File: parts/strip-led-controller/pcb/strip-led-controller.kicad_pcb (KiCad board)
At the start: 2 copper layers, 100.5 x 48 mm, 18 parts, among them J1 BUCK_IN, J2 PWR IN, J3 BUCK_OUT, SW2 SW_SPDT, U1 ESP32 Wemos D1 Mini

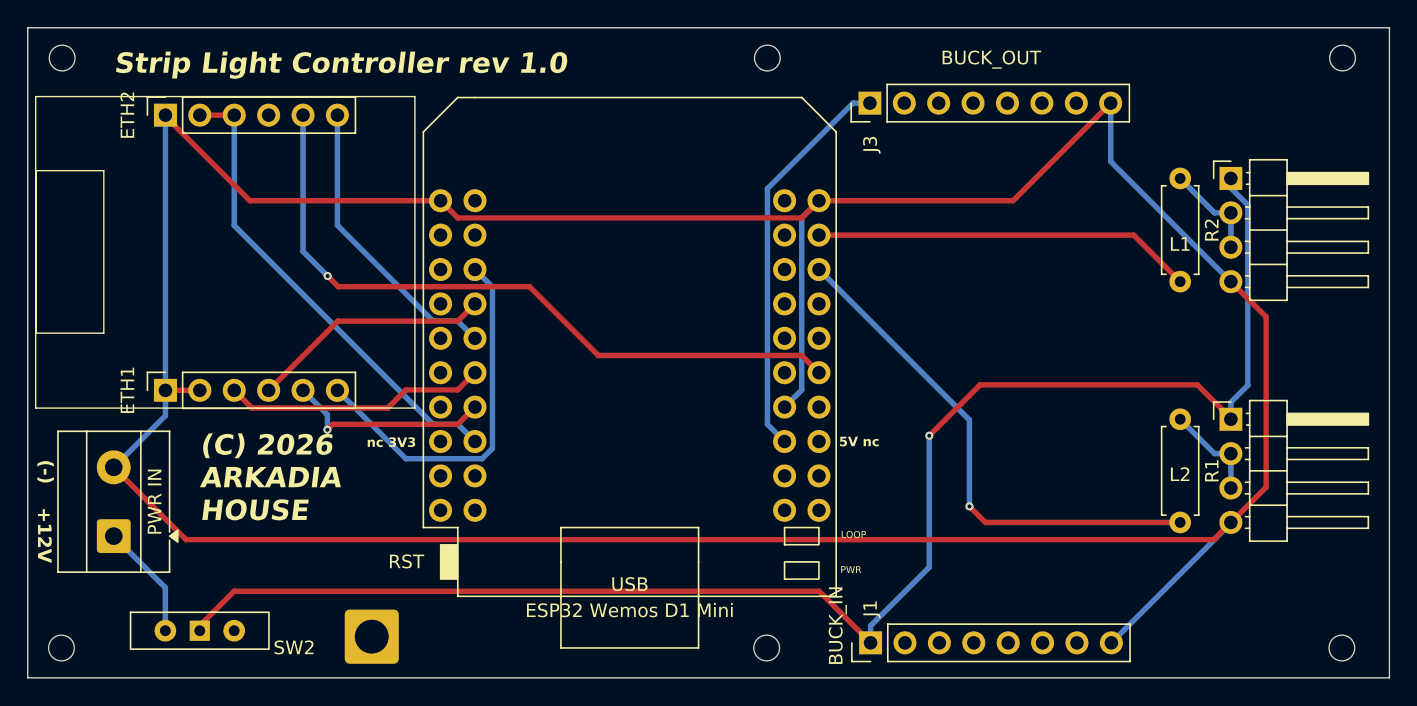
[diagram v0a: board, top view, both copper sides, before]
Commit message: update RJ45 connector to "clip up" model
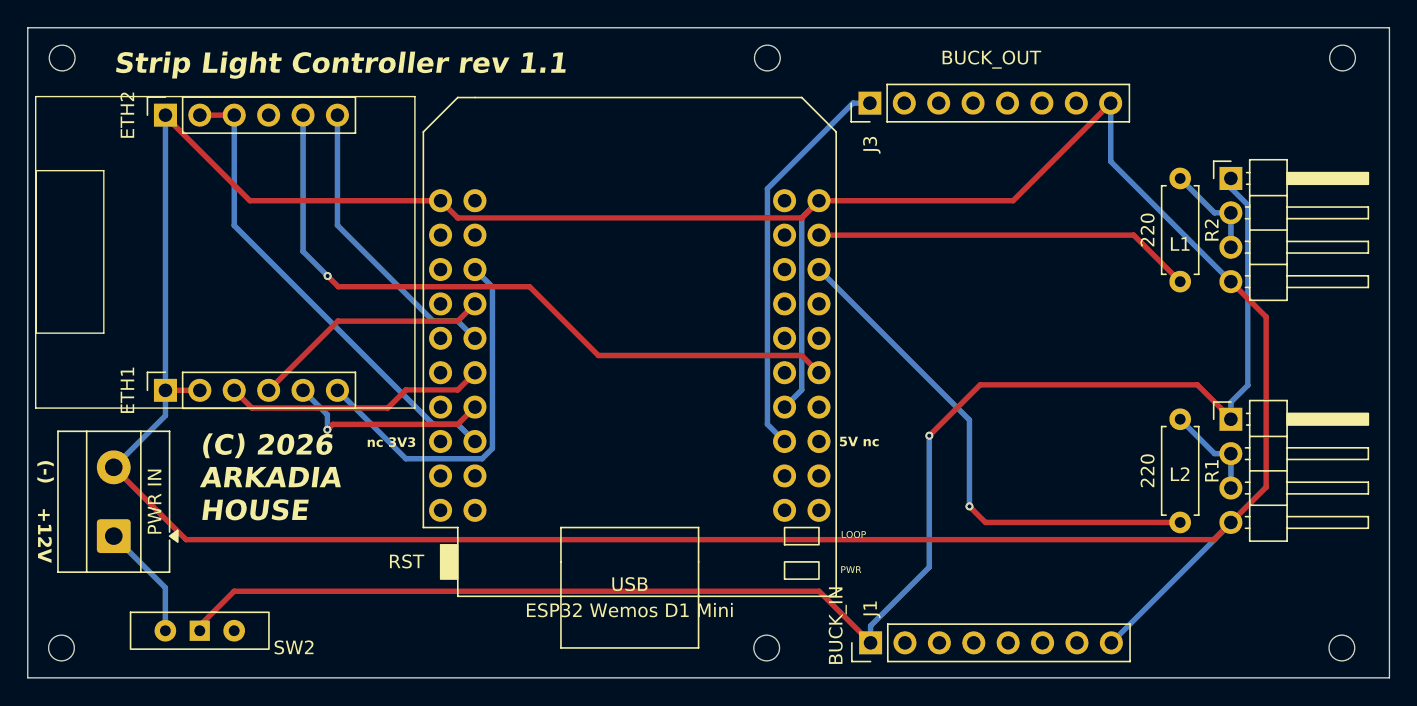
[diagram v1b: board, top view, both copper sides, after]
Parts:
- removed SHIELD1: Conn_01x01_Shielded, TerminalBlock:TerminalBlock_MaiXu_MX126-5.0-02P_1x02_P5.00mm
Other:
- board text added: "Strip Light Controller rev 1.1"
- board text removed: "Strip Light Controller rev 1.0"

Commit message: pixelstrip controller 1.2 adjusts small geometry and labeling based on assembly esperience.
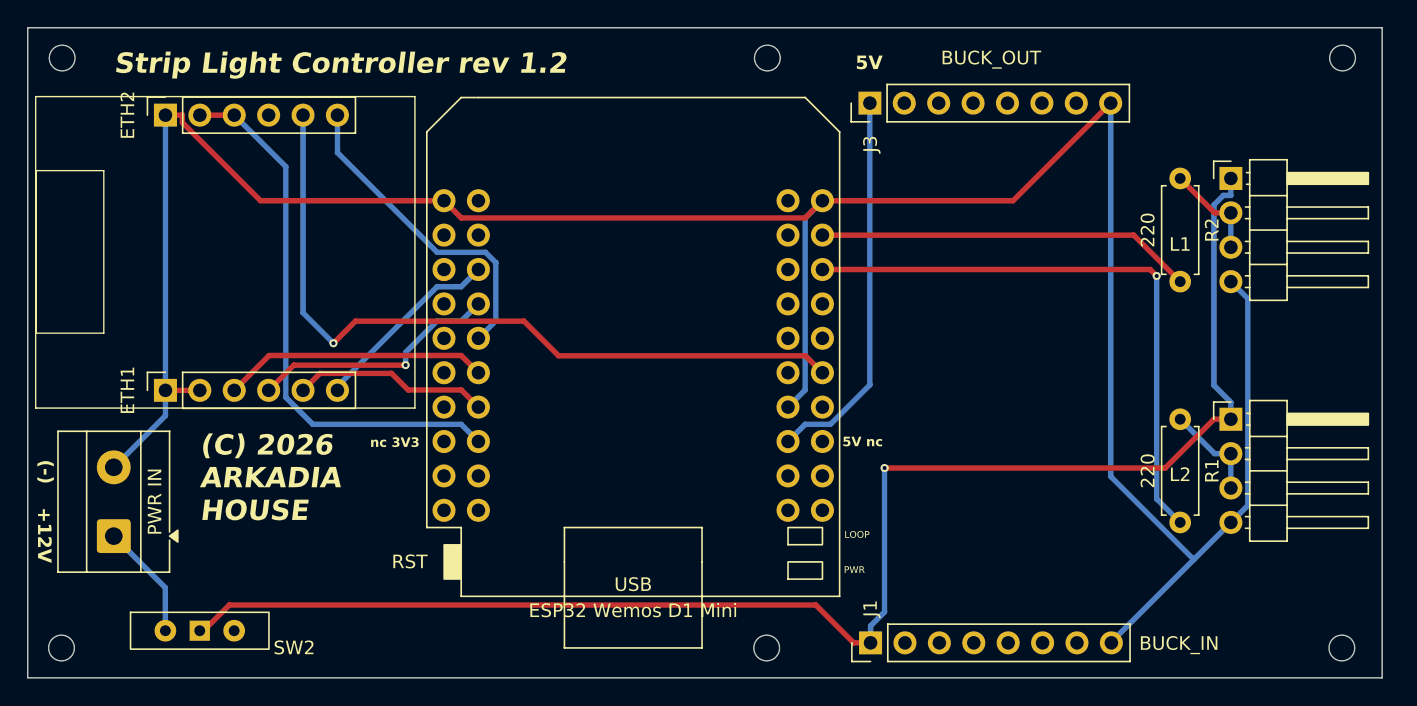
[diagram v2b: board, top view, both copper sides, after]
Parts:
- moved U1 0.25 mm to (68.2, 46.4)
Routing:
- net GND: track 257.4 -> 190.7 mm
- net /INT: track 27.6 -> 14.0 mm
- net Net-(U1-IO_25): track 38.1 -> 43.8 mm
- net /3V3: track 35.1 -> 40.5 mm
- net Net-(ETH2-RST): track 51.9 -> 56.1 mm
- net /12V: track 112.9 -> 110.4 mm
- net Net-(ETH2-MISO): track 21.7 -> 23.9 mm
- net /SCK: track 17.9 -> 18.7 mm, vias 0 -> 1
- net /5V: track 29.4 -> 28.6 mm
- net /CS: track 15.2 -> 14.5 mm, vias 1 -> 0
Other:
- board size 100.5 x 48 mm -> 100 x 48 mm
- board text added: "12V"
- board text added: "3V3"
- board text added: "5V"
- board text added: "GND"
- board text added: "Strip Light Controller rev 1.2"
- board text removed: "Strip Light Controller rev 1.1"
